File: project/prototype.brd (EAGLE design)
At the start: 0 parts

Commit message: Add components
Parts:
- added U$1, U$5, U$9: RJ12, components:RJ12
- added U$10, U$11, U$2, U$3, U$6, U$7: CPC1017N, components:SOP-4
- added U$12, U$4, U$8: NX7002AK, components:SOT23
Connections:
- new net N$1: U$1.1, U$2.3
- new net N$10: U$11.4, U$5.4, U$7.3, U$9.2
- new net N$11: U$6.1, U$7.1
- new net N$12: U$6.2, U$7.2
- new net N$15: U$10.4, U$9.3
- new net N$16: U$11.3, U$9.4
- new net N$17: U$10.1, U$11.1
- new net N$18: U$10.2, U$11.2
- new net N$2: U$1.2, U$3.4
- new net N$3: U$1.3, U$2.4, U$5.1, U$6.3
- new net N$4: U$1.4, U$3.3, U$5.2, U$7.4
- new net N$5: U$2.1, U$3.1
- new net N$7: U$2.2, U$3.2
- new net N$9: U$10.3, U$5.3, U$6.4, U$9.1
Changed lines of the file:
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@@
 <setting verticaltext="up"/>
 </settings>
-<grid distance="50" unitdist="mil" unit="mil" style="lines" multiple="1" display="no" altdistance="5" altunitdist="mil" altunit="mil"/>
+<grid distance="50" unitdist="mil" unit="mil" style="lines" multiple="1" display="yes" altdistance="5" altunitdist="mil" altunit="mil"/>
 <layers>
 <layer number="1" name="Top" color="4" fill="1" visible="yes" active="yes"/>
@@
 <layer number="51" name="tDocu" color="7" fill="1" visible="yes" active="yes"/>
 <layer number="52" name="bDocu" color="7" fill="1" visible="yes" active="yes"/>
+<layer number="88" name="SimResults" color="9" fill="1" visible="no" active="no"/>
+<layer number="89" name="SimProbes" color="9" fill="1" visible="no" active="no"/>
+<layer number="90" name="Modules" color="5" fill="1" visible="no" active="no"/>
+<layer number="91" name="Nets" color="2" fill="1" visible="no" active="no"/>
+<layer number="92" name="Busses" color="1" fill="1" visible="no" active="no"/>
+<layer number="93" name="Pins" color="2" fill="1" visible="no" active="no"/>
+<layer number="94" name="Symbols" color="4" fill="1" visible="no" active="no"/>
+<layer number="95" name="Names" color="7" fill="1" visible="no" active="no"/>
+<layer number="96" name="Values" color="7" fill="1" visible="no" active="no"/>
+<layer number="97" name="Info" color="7" fill="1" visible="no" active="no"/>
+<layer number="98" name="Guide" color="6" fill="1" visible="no" active="no"/>
 </layers>
 <board>
@@
 </autorouter>
 <elements>
+<element name="U$1" library="components" package="RJ12" value="RJ12" x="17.78" y="0" smashed="yes" rot="R180">
+<attribute name="NAME" x="17.78" y="2" size="1.27" layer="21" font="vector" rot="R180" align="center"/>
+<attribute name="VALUE" x="17.78" y="4" size="0.889" layer="21" font="vector" rot="R180" align="center"/>
+</element>
+<element name="U$2" library="components" package="SOP-4" value="CPC1017N" x="15.24" y="21.59" smashed="yes" rot="R270">
+<attribute name="NAME" x="15.875" y="21.59" size="0.889" layer="25" font="vector" rot="R270" align="center"/>
+<attribute name="VALUE" x="14.605" y="21.59" size="0.635" layer="27" font="vector" rot="R270" align="center"/>
+</element>
+<element name="U$3" library="components" package="SOP-4" value="CPC1017N" x="20.32" y="21.59" smashed="yes" rot="R270">
+<attribute name="NAME" x="20.955" y="21.59" size="0.889" layer="25" font="vector" rot="R270" align="center"/>
+<attribute name="VALUE" x="19.685" y="21.59" size="0.635" layer="27" font="vector" rot="R270" align="center"/>
+</element>
+<element name="U$4" library="components" package="SOT23" value="NX7002AK" x="20.32" y="29.21" smashed="yes">
+<attribute name="NAME" x="20.32" y="29.46" size="0.35" layer="25" font="vector" rot="R180" align="center"/>
+<attribute name="VALUE" x="20.32" y="28.96" size="0.25" layer="27" font="vector" rot="R180" align="center"/>
+</element>
+<element name="U$5" library="components" package="RJ12" value="RJ12" x="33.02" y="0" smashed="yes" rot="R180">
+<attribute name="NAME" x="33.02" y="2" size="1.27" layer="21" font="vector" rot="R180" align="center"/>
+<attribute name="VALUE" x="33.02" y="4" size="0.889" layer="21" font="vector" rot="R180" align="center"/>
+</element>
+<element name="U$6" library="components" package="SOP-4" value="CPC1017N" x="30.48" y="21.59" smashed="yes" rot="R270">
+<attribute name="NAME" x="31.115" y="21.59" size="0.889" layer="25" font="vector" rot="R270" align="center"/>
+<attribute name="VALUE" x="29.845" y="21.59" size="0.635" layer="27" font="vector" rot="R270" align="center"/>
+</element>
+<element name="U$7" library="components" package="SOP-4" value="CPC1017N" x="35.56" y="21.59" smashed="yes" rot="R270">
+<attribute name="NAME" x="36.195" y="21.59" size="0.889" layer="25" font="vector" rot="R270" align="center"/>
+<attribute name="VALUE" x="34.925" y="21.59" size="0.635" layer="27" font="vector" rot="R270" align="center"/>
+</element>
+<element name="U$8" library="components" package="SOT23" value="NX7002AK" x="35.56" y="29.21" smashed="yes">
+<attribute name="NAME" x="35.56" y="29.46" size="0.35" layer="25" font="vector" rot="R180" align="center"/>
+<attribute name="VALUE" x="35.56" y="28.96" size="0.25" layer="27" font="vector" rot="R180" align="center"/>
+</element>
+<element name="U$9" library="components" package="RJ12" value="RJ12" x="48.26" y="0" smashed="yes" rot="R180">
+<attribute name="NAME" x="48.26" y="2" size="1.27" layer="21" font="vector" rot="R180" align="center"/>
+<attribute name="VALUE" x="48.26" y="4" size="0.889" layer="21" font="vector" rot="R180" align="center"/>
+</element>
+<element name="U$10" library="components" package="SOP-4" value="CPC1017N" x="45.72" y="21.59" smashed="yes" rot="R270">
+<attribute name="NAME" x="46.355" y="21.59" size="0.889" layer="25" font="vector" rot="R270" align="center"/>
+<attribute name="VALUE" x="45.085" y="21.59" size="0.635" layer="27" font="vector" rot="R270" align="center"/>
+</element>
+<element name="U$11" library="components" package="SOP-4" value="CPC1017N" x="50.8" y="21.59" smashed="yes" rot="R270">
+<attribute name="NAME" x="51.435" y="21.59" size="0.889" layer="25" font="vector" rot="R270" align="center"/>
+<attribute name="VALUE" x="50.165" y="21.59" size="0.635" layer="27" font="vector" rot="R270" align="center"/>
+</element>
+<element name="U$12" library="components" package="SOT23" value="NX7002AK" x="50.8" y="29.21" smashed="yes">
+<attribute name="NAME" x="50.8" y="29.46" size="0.35" layer="25" font="vector" rot="R180" align="center"/>
+<attribute name="VALUE" x="50.8" y="28.96" size="0.25" layer="27" font="vector" rot="R180" align="center"/>
+</element>
 </elements>
 <signals>
+<signal name="N$1">
+<contactref element="U$1" pad="1"/>
+<contactref element="U$2" pad="3"/>
+<wire x1="14.605" y1="15.39" x2="13.97" y2="18.84" width="0" layer="19" extent="1-1"/>
+</signal>
+<signal name="N$2">
+<contactref element="U$1" pad="2"/>
+<contactref element="U$3" pad="4"/>
+<wire x1="15.875" y1="12.85" x2="21.59" y2="18.84" width="0" layer="19" extent="1-1"/>
+</signal>
+<signal name="N$3">
+<contactref element="U$1" pad="3"/>
+<contactref element="U$2" pad="4"/>
+<contactref element="U$5" pad="1"/>
+<contactref element="U$6" pad="3"/>
+<wire x1="29.845" y1="15.39" x2="29.21" y2="18.84" width="0" layer="19" extent="1-1"/>
+<wire x1="17.145" y1="15.39" x2="29.845" y2="15.39" width="0" layer="19" extent="1-1"/>
+<wire x1="16.51" y1="18.84" x2="17.145" y2="15.39" width="0" layer="19" extent="1-1"/>
+</signal>
+<signal name="N$4">
+<contactref element="U$1" pad="4"/>
+<contactref element="U$3" pad="3"/>
+<contactref element="U$5" pad="2"/>
+<contactref element="U$7" pad="4"/>
+<wire x1="36.83" y1="18.84" x2="31.115" y2="12.85" width="0" layer="19" extent="1-1"/>
+<wire x1="18.415" y1="12.85" x2="31.115" y2="12.85" width="0" layer="19" extent="1-1"/>
+<wire x1="19.05" y1="18.84" x2="18.415" y2="12.85" width="0" layer="19" extent="1-1"/>
+</signal>
+<signal name="N$5">
+<contactref element="U$2" pad="1"/>
+<contactref element="U$3" pad="1"/>
+<wire x1="16.51" y1="24.34" x2="21.59" y2="24.34" width="0" layer="19" extent="1-1"/>
+</signal>
+<signal name="N$7">
+<contactref element="U$2" pad="2"/>
+<contactref element="U$3" pad="2"/>
+<wire x1="13.97" y1="24.34" x2="19.05" y2="24.34" width="0" layer="19" extent="1-1"/>
+</signal>
+<signal name="N$9">
+<contactref element="U$5" pad="3"/>
+<contactref element="U$6" pad="4"/>
+<contactref element="U$9" pad="1"/>
+<contactref element="U$10" pad="3"/>
+<wire x1="45.085" y1="15.39" x2="44.45" y2="18.84" width="0" layer="19" extent="1-1"/>
+<wire x1="31.75" y1="18.84" x2="45.085" y2="15.39" width="0" layer="19" extent="1-1"/>
+<wire x1="32.385" y1="15.39" x2="31.75" y2="18.84" width="0" layer="19" extent="1-1"/>
+</signal>
+<signal name="N$10">
+<contactref element="U$5" pad="4"/>
+<contactref element="U$7" pad="3"/>
+<contactref element="U$9" pad="2"/>
+<contactref element="U$11" pad="4"/>
+<wire x1="52.07" y1="18.84" x2="46.355" y2="12.85" width="0" layer="19" extent="1-1"/>
+<wire x1="34.29" y1="18.84" x2="46.355" y2="12.85" width="0" layer="19" extent="1-1"/>
+<wire x1="33.655" y1="12.85" x2="34.29" y2="18.84" width="0" layer="19" extent="1-1"/>
+</signal>
+<signal name="N$11">
+<contactref element="U$6" pad="1"/>
+<contactref element="U$7" pad="1"/>
+<wire x1="36.83" y1="24.34" x2="31.75" y2="24.34" width="0" layer="19" extent="1-1"/>
+</signal>
+<signal name="N$12">
+<contactref element="U$6" pad="2"/>
+<contactref element="U$7" pad="2"/>
+<wire x1="34.29" y1="24.34" x2="29.21" y2="24.34" width="0" layer="19" extent="1-1"/>
+</signal>
+<signal name="N$15">
+<contactref element="U$9" pad="3"/>
+<contactref element="U$10" pad="4"/>
+<wire x1="47.625" y1="15.39" x2="46.99" y2="18.84" width="0" layer="19" extent="1-1"/>
+</signal>
+<signal name="N$16">
+<contactref element="U$9" pad="4"/>
+<contactref element="U$11" pad="3"/>
+<wire x1="49.53" y1="18.84" x2="48.895" y2="12.85" width="0" layer="19" extent="1-1"/>
+</signal>
+<signal name="N$17">
+<contactref element="U$10" pad="1"/>
+<contactref element="U$11" pad="1"/>
+<wire x1="52.07" y1="24.34" x2="46.99" y2="24.34" width="0" layer="19" extent="1-1"/>
+</signal>
+<signal name="N$18">
+<contactref element="U$10" pad="2"/>
+<contactref element="U$11" pad="2"/>
+<wire x1="49.53" y1="24.34" x2="44.45" y2="24.34" width="0" layer="19" extent="1-1"/>
+</signal>
 </signals>
 <mfgpreviewcolors>

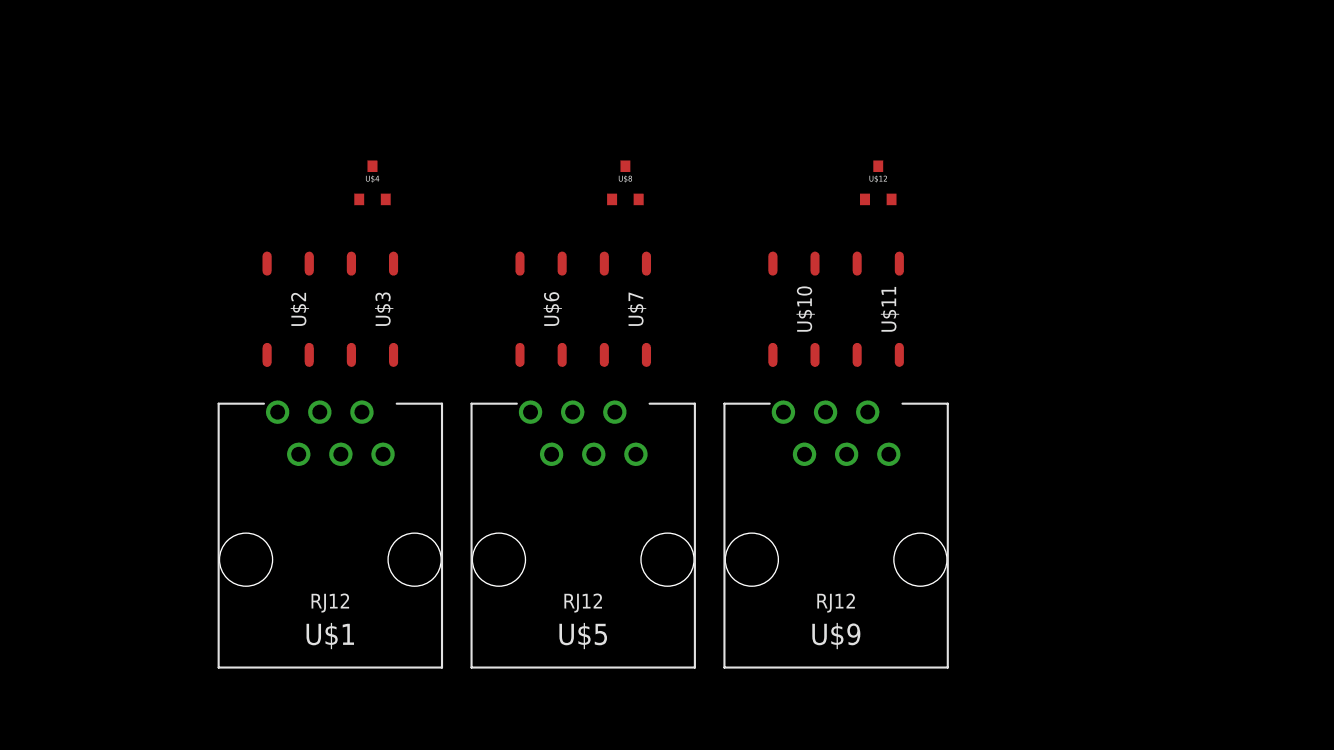
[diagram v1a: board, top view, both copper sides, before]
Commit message: Add red LED
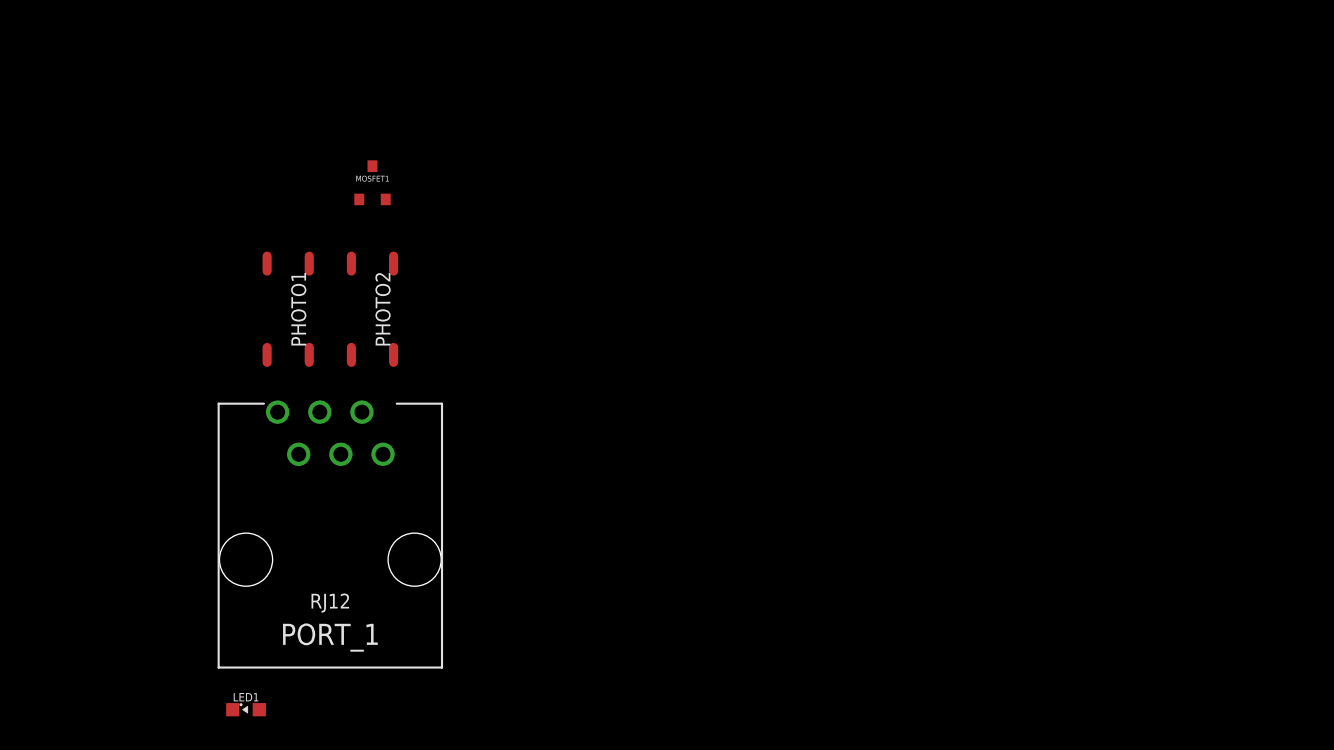
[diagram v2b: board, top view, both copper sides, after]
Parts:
- removed U$10, U$11, U$6, U$7: CPC1017N, components:SOP-4
- removed U$12, U$8: NX7002AK, components:SOT23
- removed U$5, U$9: RJ12, components:RJ12
- added LED1: RED, components:0603-LED
- renumbered U$1 to PORT_1, U$2 to PHOTO1, U$3 to PHOTO2, U$4 to MOSFET1
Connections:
- removed net N$10: U$11.4, U$5.4, U$7.3, U$9.2
- removed net N$11: U$6.1, U$7.1
- removed net N$12: U$6.2, U$7.2
- removed net N$15: U$10.4, U$9.3
- removed net N$16: U$11.3, U$9.4
- removed net N$17: U$10.1, U$11.1
- removed net N$18: U$10.2, U$11.2
- removed net N$3 (its old number): PHOTO1.4, PORT_1.3, U$5.1, U$6.3
- removed net N$9: U$10.3, U$5.3, U$6.4, U$9.1
- new net GND: MOSFET1.2, PORT_1.6
- new net N$2: PHOTO1.3, PORT_1.3
- new net N$5: MOSFET1.1, PORT_1.5
- new net N$8: LED1.1, MOSFET1.3
- net N$1: now also PHOTO1.4; no longer PHOTO1.3
- net N$4: no longer U$5.2, U$7.4
- net N$7: now also LED1.2

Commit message: Add indicator LED layout
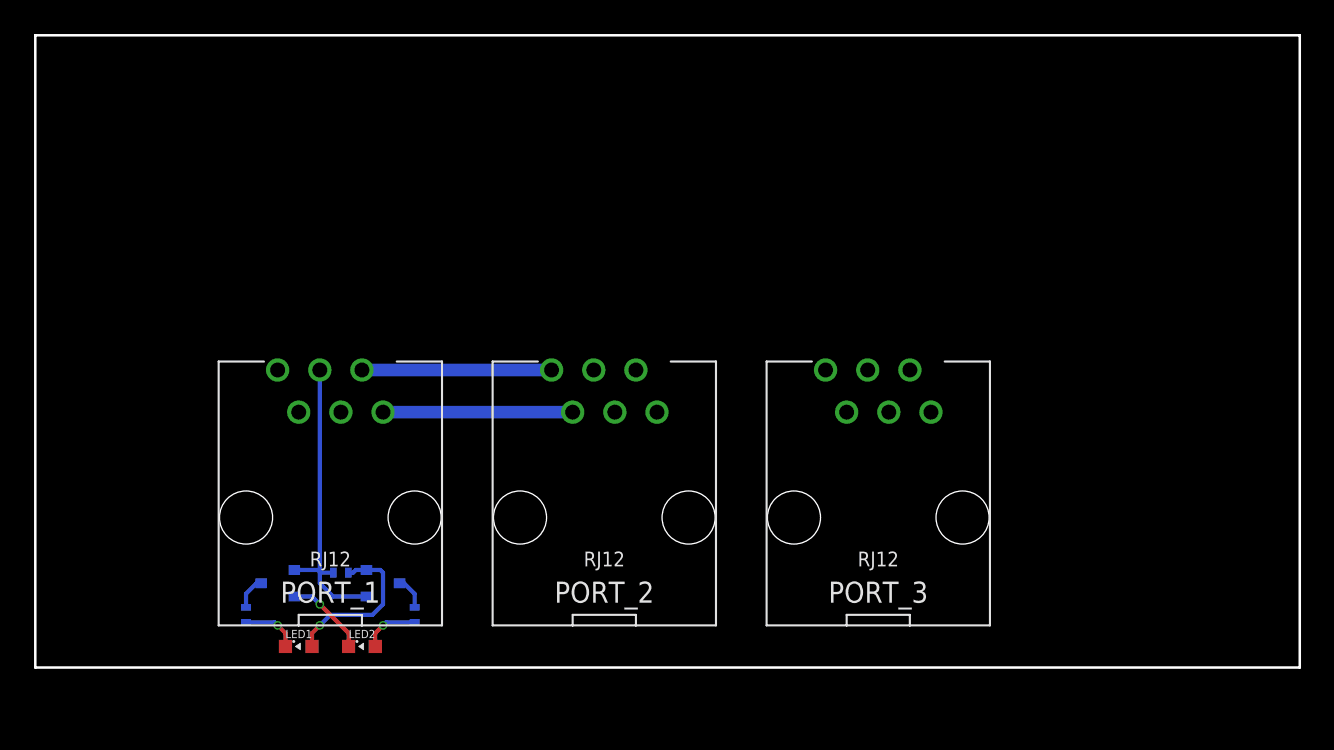
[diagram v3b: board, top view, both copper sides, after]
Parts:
- removed MOSFET1: NX7002AK, components:SOT23
- removed PHOTO1, PHOTO2: CPC1017N, components:SOP-4
- added LED2: GREEN, components:0603-LED
- added M1: NX7002AK, components:SOT23
- added M2: NX3008PBK, components:SOT23
- added PORT_2, PORT_3: RJ12, components:RJ12
- added R1, R2: 130, components:0402
- added R3: 10K, components:0402
- moved LED1 4.96 mm to (15.9, 1.27)
- moved PORT_1 2.54 mm to (17.8, 2.54)
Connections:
- new net +5V: LED1.2, M2.2, R3.2
- new net CAN-H: PORT_1.1
- new net CAN-L: PORT_1.2
- new net GATE: M1.1, M2.1, PORT_1.3, R3.1
- new net N$10: LED2.2, R2.1
- new net N$9: PORT_3.6
- net GND: now also LED2.1, M1.2, PORT_1.4, PORT_3.4; no longer MOSFET1.2, PORT_1.6
- net N$1: now also LED1.1, R1.1; no longer PHOTO1.4, PORT_1.1
- net N$2: now also M1.3, R1.2; no longer PHOTO1.3, PORT_1.3
- net N$3: now also PORT_1.5, PORT_2.1; no longer PHOTO2.4, PORT_1.2
- net N$4: now also M2.3, R2.2; no longer PHOTO2.3, PORT_1.4
- net N$5: now also PORT_3.5; no longer MOSFET1.1, PORT_1.5
- net N$6: now also PORT_1.6, PORT_2.2; no longer PHOTO1.1, PHOTO2.1
- net N$7: now also PORT_2.5, PORT_3.1; no longer LED1.2, PHOTO1.2, PHOTO2.2
- net N$8: now also PORT_2.6, PORT_3.2; no longer LED1.1, MOSFET1.3
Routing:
- net GATE: track 0.00 -> 18.4 mm
- net N$6: track 0.00 -> 11.4 mm
- net N$3: track 0.00 -> 11.4 mm
- net +5V: track 0.00 -> 9.93 mm, vias 0 -> 1
- net GND: track 0.00 -> 5.00 mm, vias 0 -> 1
- net N$1: track 0.00 -> 3.45 mm, vias 0 -> 1
- net N$10: track 0.00 -> 3.45 mm, vias 0 -> 1
- net N$4: track 0.00 -> 1.99 mm
- net N$2: track 0.00 -> 1.99 mm
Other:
- board outline added: 76.2 x 38.1 mm
